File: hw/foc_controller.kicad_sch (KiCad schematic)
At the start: 8 parts

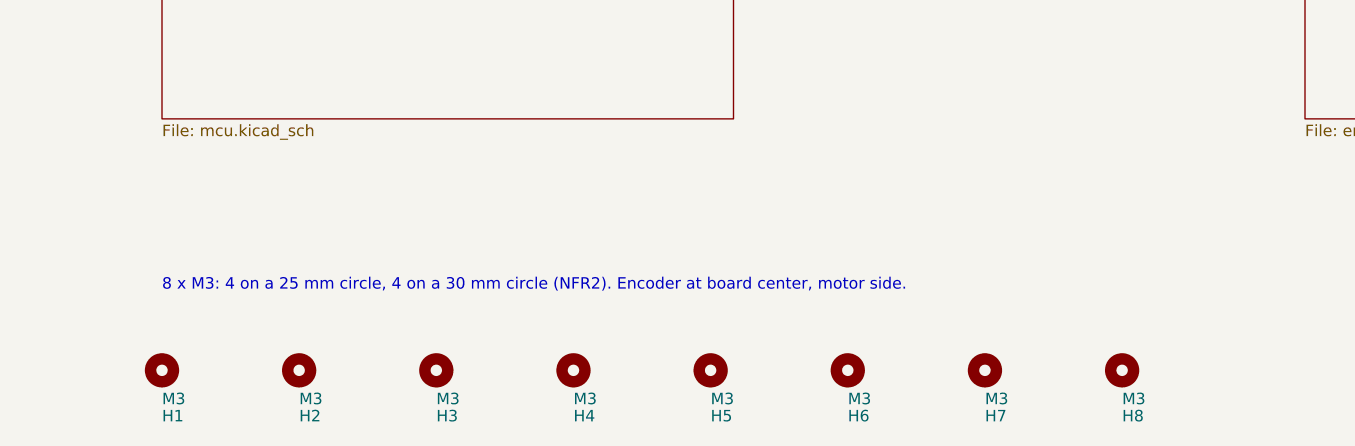
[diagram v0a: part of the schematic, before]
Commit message: Remove requirement IDs from schematic notes
Notes now state the reason in plain words so the schematic reads
without the requirements document.

Co-Authored-By: Claude Opus 5.5 <noreply@anthropic.com>
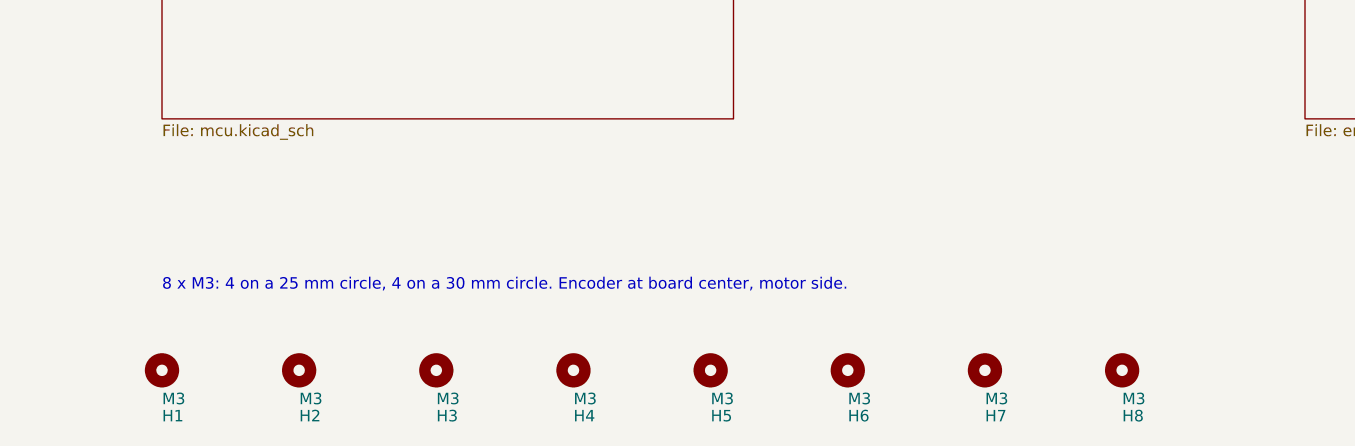
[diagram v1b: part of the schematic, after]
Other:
- note added: "8 x M3: 4 on a 25 mm circle, 4 on a 30 mm circle. Encoder at board center, motor side."
- note removed: "8 x M3: 4 on a 25 mm circle, 4 on a 30 mm circle (NFR2). Encoder at board center, motor side."
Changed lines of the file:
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@@
 		)
 	)
-	(text "8 x M3: 4 on a 25 mm circle, 4 on a 30 mm circle (NFR2). Encoder at board center, motor side."
+	(text "8 x M3: 4 on a 25 mm circle, 4 on a 30 mm circle. Encoder at board center, motor side."
 		(exclude_from_sim no)
 		(at 50.8 264.16 0.0000)

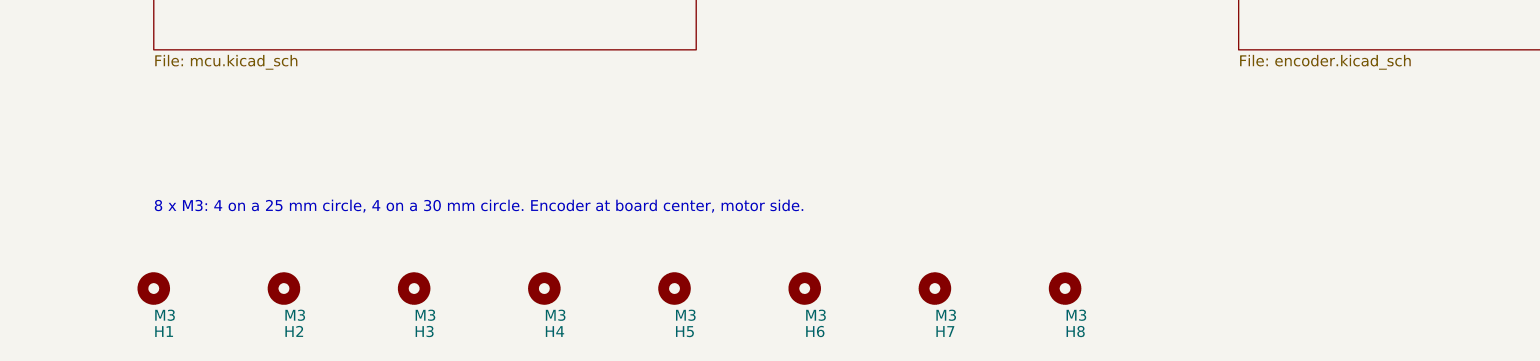
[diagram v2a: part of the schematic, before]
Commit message: Place the 45 x 45 mm two-sided board and review its risks
Ceramic-only bulk caps, per-phase caps under each FET pair, one FET row,
corner M3 holes, USB-C and CAN on the motor side, XT30s closer together.
Encoder clearance 10 mm, 10 A RMS rating with no heatsink. Placement
fixes from the risk review: BOOT0 pad away from VBUS, 3 mm clear around
the XT30 power joints, edge caps parallel to the edge. Specs, layout
check and risk review updated; fuse and regen clamp now required
off-board parts.

Co-Authored-By: Claude Opus 5.5 <noreply@anthropic.com>
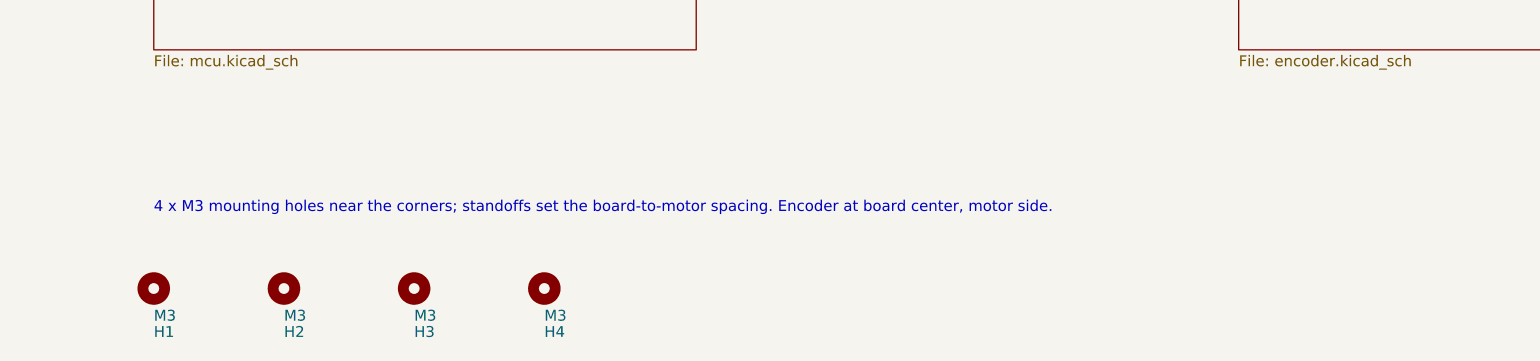
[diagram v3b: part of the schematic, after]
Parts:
- removed H5, H6, H7, H8: M3, MountingHole:MountingHole_3.2mm_M3, symbol Mechanical:MountingHole
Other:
- note added: "4 x M3 mounting holes near the corners; standoffs set the board-to-motor spacing. Encoder at board center, motor side."
- note removed: "8 x M3: 4 on a 25 mm circle, 4 on a 30 mm circle. Encoder at board center, motor side."

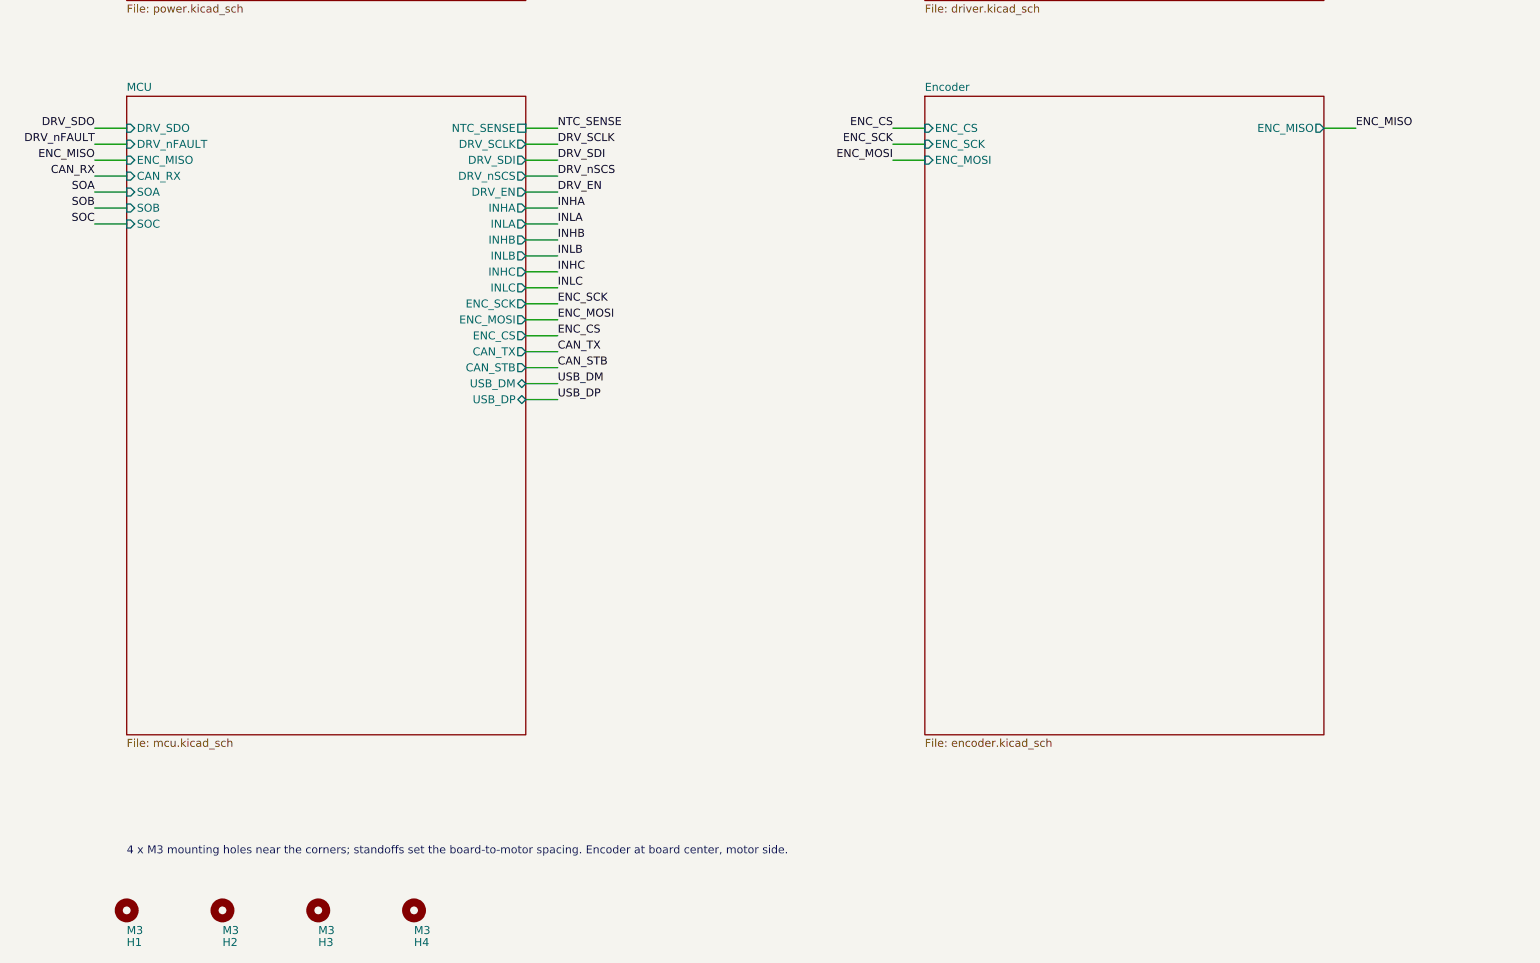
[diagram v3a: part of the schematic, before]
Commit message: Route the 6-layer board and finalize parts for ordering
The 45 x 45 mm board is fully routed on six layers (F / GND / SIG /
SIG / PWR / B, 2 oz outer, 1 oz inner): DRC 0 errors, 0 unconnected,
schematic parity 0. Four layers could not route the DRV-to-MCU links
without moving the power or input stage.

- Encoder shares the DRV8353's SPI3 bus, as on the PoC; PA5-PA7 are
  unused. R25 pulls DRV nSCS up, since the DRV's logic inputs have an
  internal pull-down. The SDO / MISO pin-type warning is an ERC
  exclusion with a note.
- MCU is now the STM32G473CEU6: the G474 without the unused HRTIM,
  checked pin for pin against both datasheets, in stock and cheaper.
- Male XT30PW-M power connectors, HCS1206 shunts, SWD pads at the
  board edge.
- Design doc and review notes updated for the new stack-up, shared
  bus and MCU.

Co-Authored-By: Claude Opus 5.5 <noreply@anthropic.com>
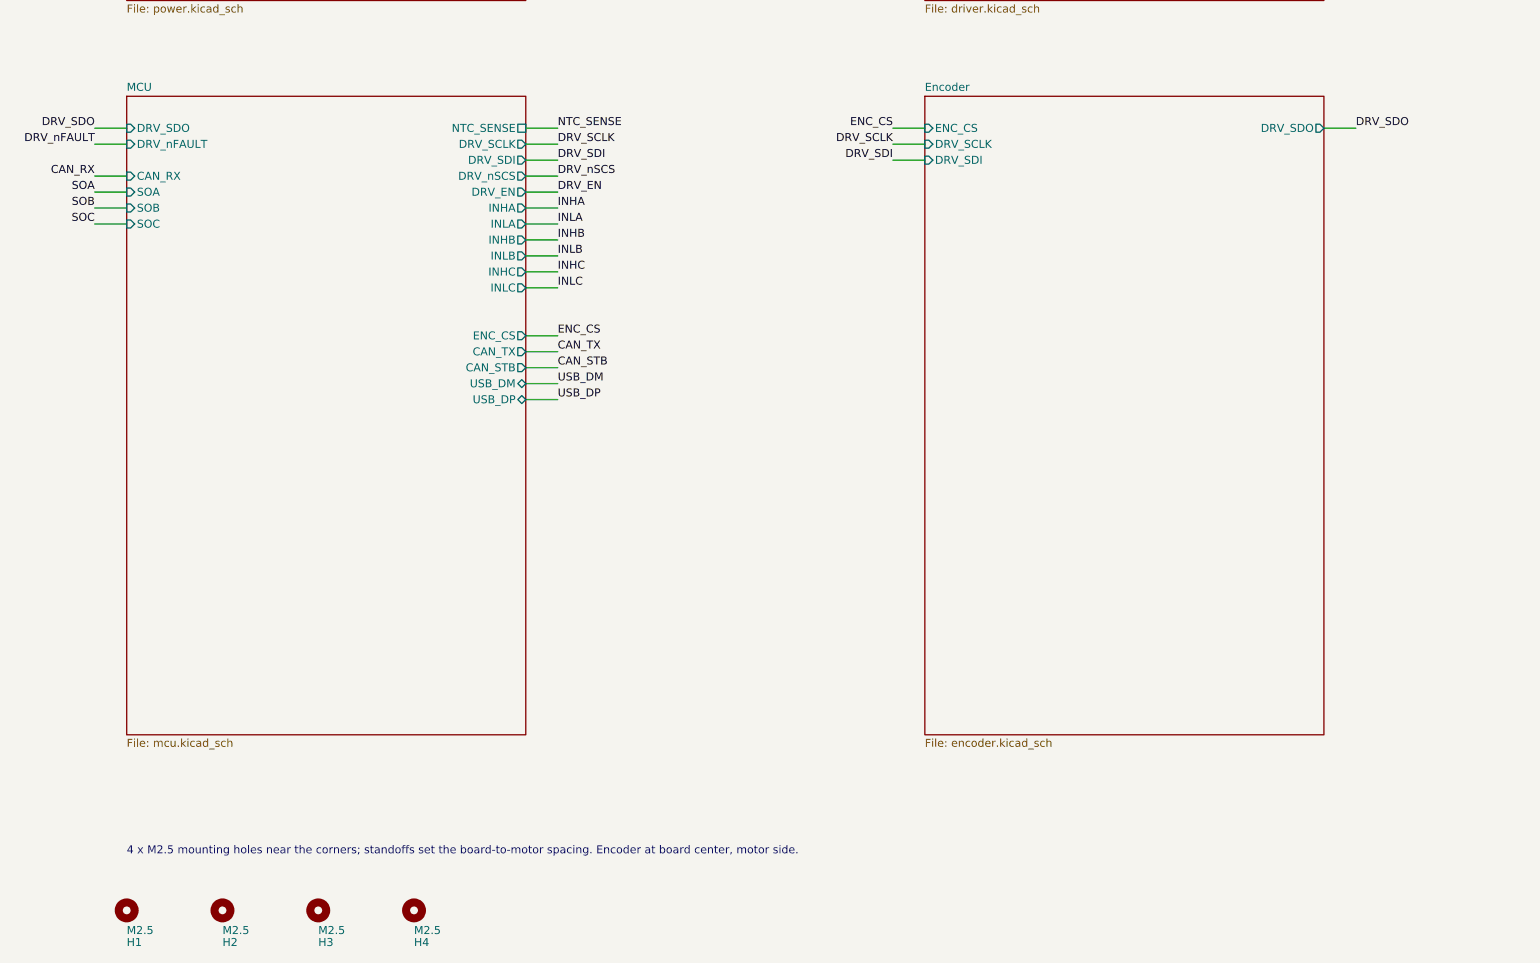
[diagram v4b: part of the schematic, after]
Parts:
- H1, H2, H3, H4: value M3 -> M2.5; footprint MountingHole:MountingHole_3.2mm_M3 -> MountingHole:MountingHole_2.7mm_M2.5
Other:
- sheet Encoder ports: added DRV_SCLK, DRV_SDI, DRV_SDO; removed ENC_MISO, ENC_MOSI, ENC_SCK
- sheet MCU ports: added none; removed ENC_MISO, ENC_MOSI, ENC_SCK
- note added: "4 x M2.5 mounting holes near the corners; standoffs set the board-to-motor spacing. Encoder at board center, motor side."
- note removed: "4 x M3 mounting holes near the corners; standoffs set the board-to-motor spacing. Encoder at board center, motor side."
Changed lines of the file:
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@@
 		(comment 2 "specs/pmsm-controller/design-electronics.md")
 	)
-	(text "4 x M3 mounting holes near the corners; standoffs set the board-to-motor spacing. Encoder at board center, motor side."
+	(text "4 x M2.5 mounting holes near the corners; standoffs set the board-to-motor spacing. Encoder at board center, motor side."
 		(exclude_from_sim no)
 		(at 50.8 264.16 0)
@@
 	(wire
 		(pts
-			(xy 114.3 177.8) (xy 119.38 177.8)
-		)
-		(stroke
-			(width 0)
-			(type default)
-		)
-	)
-	(wire
-		(pts
 			(xy 368.3 38.1) (xy 373.38 38.1)
 		)
@@
 	(wire
 		(pts
-			(xy 114.3 180.34) (xy 119.38 180.34)
-		)
-		(stroke
-			(width 0)
-			(type default)
-		)
-	)
-	(wire
-		(pts
 			(xy 241.3 68.58) (xy 246.38 68.58)
 		)
@@
 		(pts
 			(xy 368.3 48.26) (xy 373.38 48.26)
-		)
-		(stroke
-			(width 0)
-			(type default)
-		)
-	)
-	(wire
-		(pts
-			(xy 50.8 154.94) (xy 45.72 154.94)
 		)
 		(stroke
@@
 		)
 	)
-	(label "ENC_SCK"
-		(at 119.38 177.8 0)
-		(effects
-			(font
-				(size 1.27 1.27)
-			)
-			(justify left bottom)
-		)
-	)
 	(label "INHC"
 		(at 172.72 53.34 180)
@@
 		)
 	)
-	(label "ENC_SCK"
+	(label "DRV_SCLK"
 		(at 172.72 152.4 180)
 		(effects
@@
 		)
 	)
-	(label "ENC_MOSI"
-		(at 119.38 180.34 0)
-		(effects
-			(font
-				(size 1.27 1.27)
-			)
-			(justify left bottom)
-		)
-	)
-	(label "ENC_MISO"
-		(at 45.72 154.94 180)
-		(effects
-			(font
-				(size 1.27 1.27)
-			)
-			(justify right bottom)
-		)
-	)
 	(label "INLB"
 		(at 172.72 50.8 180)
@@
 		)
 	)
-	(label "ENC_MISO"
+	(label "DRV_SDO"
 		(at 246.38 149.86 0)
 		(effects
@@
 		)
 	)
-	(label "ENC_MOSI"
+	(label "DRV_SDI"
 		(at 172.72 154.94 180)
 		(effects
@@
 			)
 		)
-		(property "Value" "M3"
+		(property "Value" "M2.5"
 			(at 50.8 277.495 0)
 			(show_name no)
@@
 			)
 		)
-		(property "Footprint" "MountingHole:MountingHole_3.2mm_M3"
+		(property "Footprint" "MountingHole:MountingHole_2.7mm_M2.5"
 			(at 50.8 274.32 0)
 			(hide yes)
@@
 			)
 		)
-		(property "Value" "M3"
+		(property "Value" "M2.5"
 			(at 66.04 277.495 0)
 			(show_name no)
@@
 			)
 		)
-		(property "Footprint" "MountingHole:MountingHole_3.2mm_M3"
+		(property "Footprint" "MountingHole:MountingHole_2.7mm_M2.5"
 			(at 66.04 274.32 0)
 			(hide yes)
@@
 			)
 		)
-		(property "Value" "M3"
+		(property "Value" "M2.5"
 			(at 96.52 277.495 0)
 			(show_name no)
@@
 			)
 		)
-		(property "Footprint" "MountingHole:MountingHole_3.2mm_M3"
+		(property "Footprint" "MountingHole:MountingHole_2.7mm_M2.5"
 			(at 96.52 274.32 0)
 			(hide yes)
@@
 			)
 		)
-		(property "Value" "M3"
+		(property "Value" "M2.5"
 			(at 81.28 277.495 0)
 			(show_name no)
@@
 			)
 		)
-		(property "Footprint" "MountingHole:MountingHole_3.2mm_M3"
+		(property "Footprint" "MountingHole:MountingHole_2.7mm_M2.5"
 			(at 81.28 274.32 0)
 			(hide yes)
@@
 			)
 		)
-		(pin "ENC_MISO" input
-			(at 50.8 154.94 180)
-			(effects
-				(font
-					(size 1.27 1.27)
-				)
-				(justify left)
-			)
-		)
 		(pin "CAN_RX" input
 			(at 50.8 157.48 180)
@@
 		(pin "INLC" output
 			(at 114.3 175.26 0)
-			(effects
-				(font
-					(size 1.27 1.27)
-				)
-				(justify right)
-			)
-		)
-		(pin "ENC_SCK" output
-			(at 114.3 177.8 0)
-			(effects
-				(font
-					(size 1.27 1.27)
-				)
-				(justify right)
-			)
-		)
-		(pin "ENC_MOSI" output
-			(at 114.3 180.34 0)
 			(effects
 				(font
@@
 			)
 		)
-		(pin "ENC_SCK" input
+		(pin "DRV_SCLK" input
 			(at 177.8 152.4 180)
 			(effects
@@
 			)
 		)
-		(pin "ENC_MOSI" input
+		(pin "DRV_SDI" input
 			(at 177.8 154.94 180)
 			(effects
@@
 			)
 		)
-		(pin "ENC_MISO" output
+		(pin "DRV_SDO" output
 			(at 241.3 149.86 0)
 			(effects
